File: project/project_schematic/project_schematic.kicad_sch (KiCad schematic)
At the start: 18 parts, among them SW1 REARM, U1 LCD-016N002L

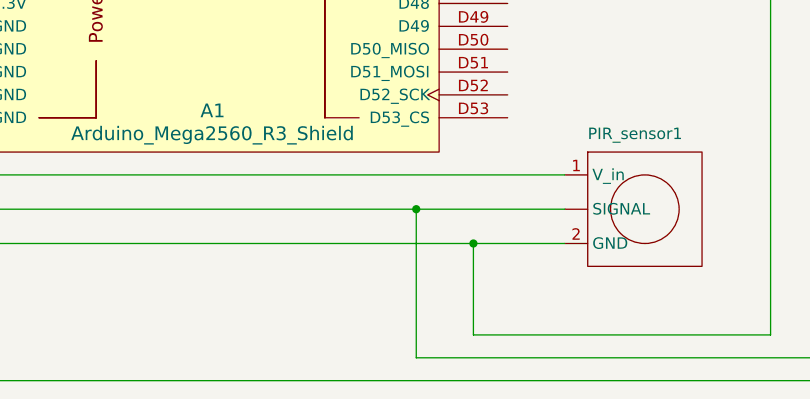
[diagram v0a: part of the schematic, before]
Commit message: Circuit schema update and video url
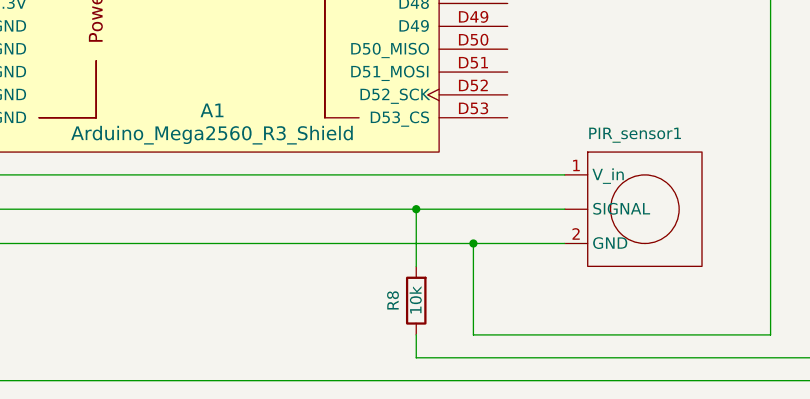
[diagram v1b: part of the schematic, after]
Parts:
- added R8: 10k, symbol Device:R
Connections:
- net at PIR_sensor1. (SIGNAL), R2.2: now also R8.2; no longer A1.D5
- new net: A1.D5, R8.1
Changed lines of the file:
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@@
 	(wire
 		(pts
-			(xy 113.03 187.96) (xy 113.03 171.45)
+			(xy 113.03 187.96) (xy 113.03 185.42)
 		)
 		(stroke
@@
 		(pts
 			(xy 39.37 120.65) (xy 57.15 120.65)
+		)
+		(stroke
+			(width 0)
+			(type default)
+		)
+	)
+	(wire
+		(pts
+			(xy 113.03 177.8) (xy 113.03 171.45)
 		)
 		(stroke
@@
 					(unit 1)
 				)
+			)
+		)
+	)
+	(symbol
+		(lib_id "Device:R")
+		(at 113.03 181.61 180)
+		(unit 1)
+		(exclude_from_sim no)
+		(in_bom yes)
+		(on_board yes)
+		(dnp no)
+		(property "Reference" "R8"
+			(at 110.49 181.61 90)
+			(effects
+				(font
+					(size 1.27 1.27)
+				)
+			)
+		)
+		(property "Value" "10k"
+			(at 113.03 181.61 90)
+			(effects
+				(font
+					(size 1.27 1.27)
+				)
+			)
+		)
+		(property "Footprint" ""
+			(at 114.808 181.61 90)
+			(effects
+				(font
+					(size 1.27 1.27)
+				)
+				(hide yes)
+			)
+		)
+		(property "Datasheet" "~"
+			(at 113.03 181.61 0)
+			(effects
+				(font
+					(size 1.27 1.27)
+				)
+				(hide yes)
+			)
+		)
+		(property "Description" "Resistor"
+			(at 113.03 181.61 0)
+			(effects
+				(font
+					(size 1.27 1.27)
+				)
+				(hide yes)
+			)
+		)
+		(pin "1"
+		)
+		(pin "2"
+		)
+		(instances
+			(project "project_schematic"
+				(path "/e93d8f61-9bc6-44b8-8b1c-4bc72ef68edc"
+					(reference "R8")
+					(unit 1)
+				)
